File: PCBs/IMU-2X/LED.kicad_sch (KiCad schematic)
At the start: 20 parts, among them Q1 DMP2004K-7, Q2 2N7002E, Q3 2N7002E, Q4 2N7002E, Q5 2N7002E

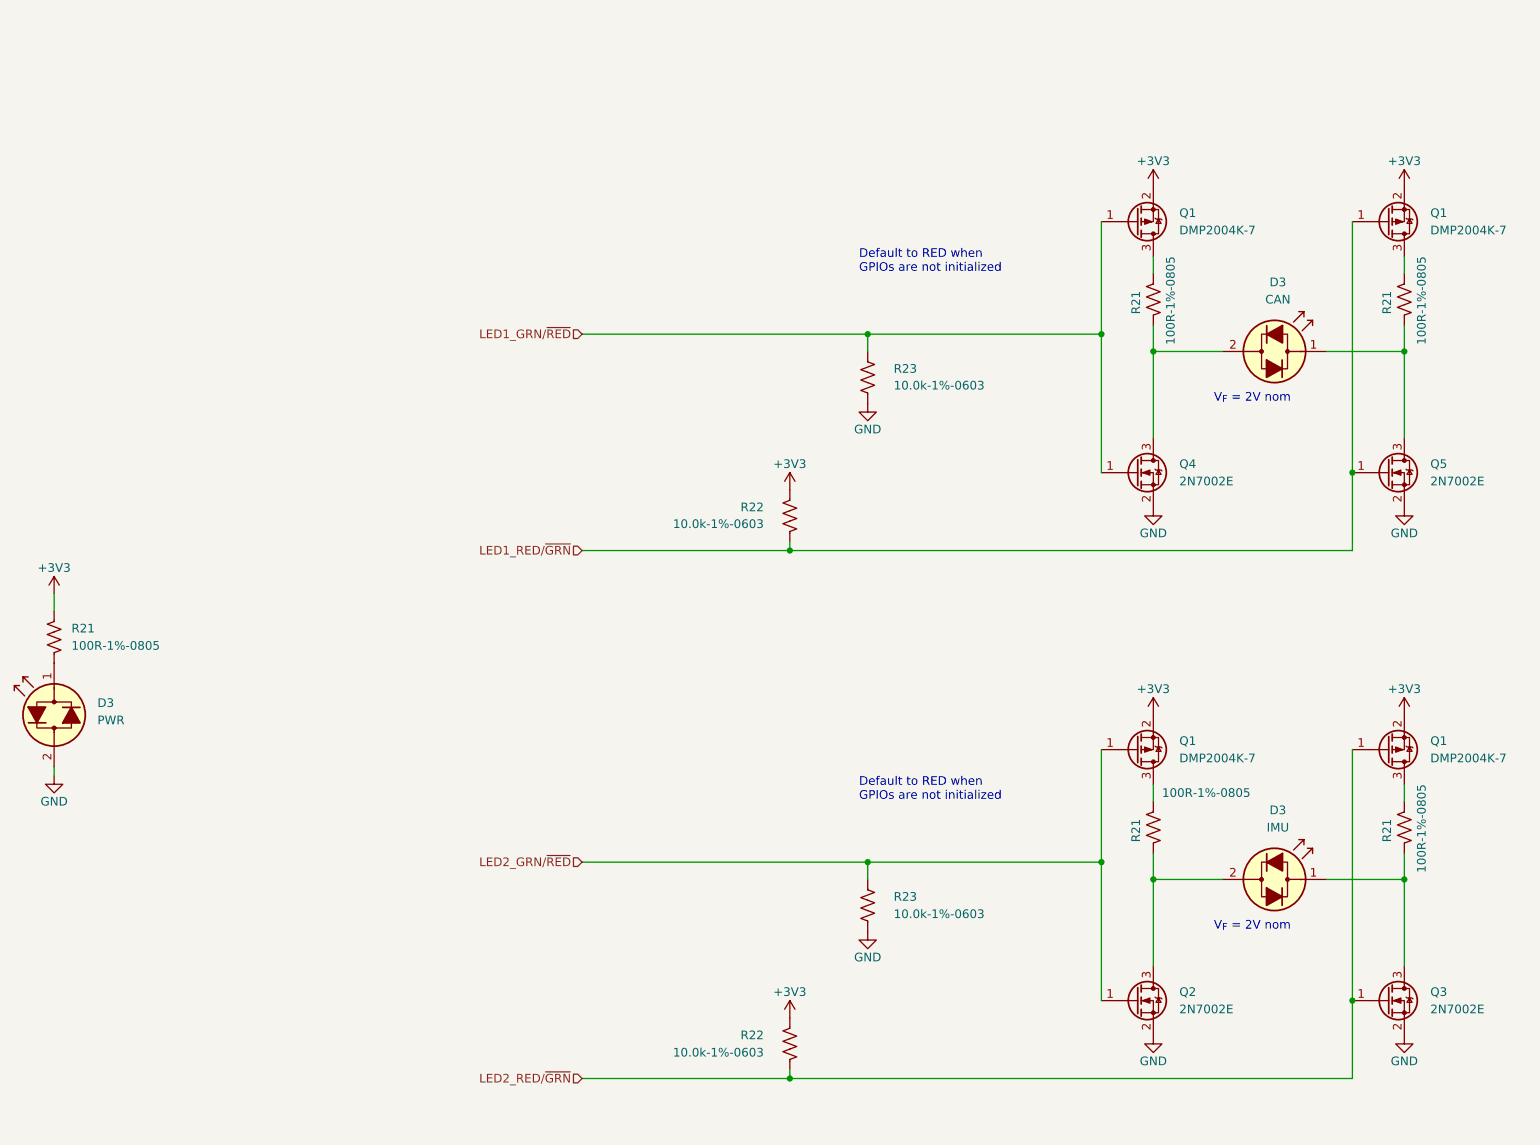
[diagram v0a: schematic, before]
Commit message: Adding IMU-2X-v2 fixes switch footprint.
Signed-off-by: Scott <sgberman1@gmail.com>
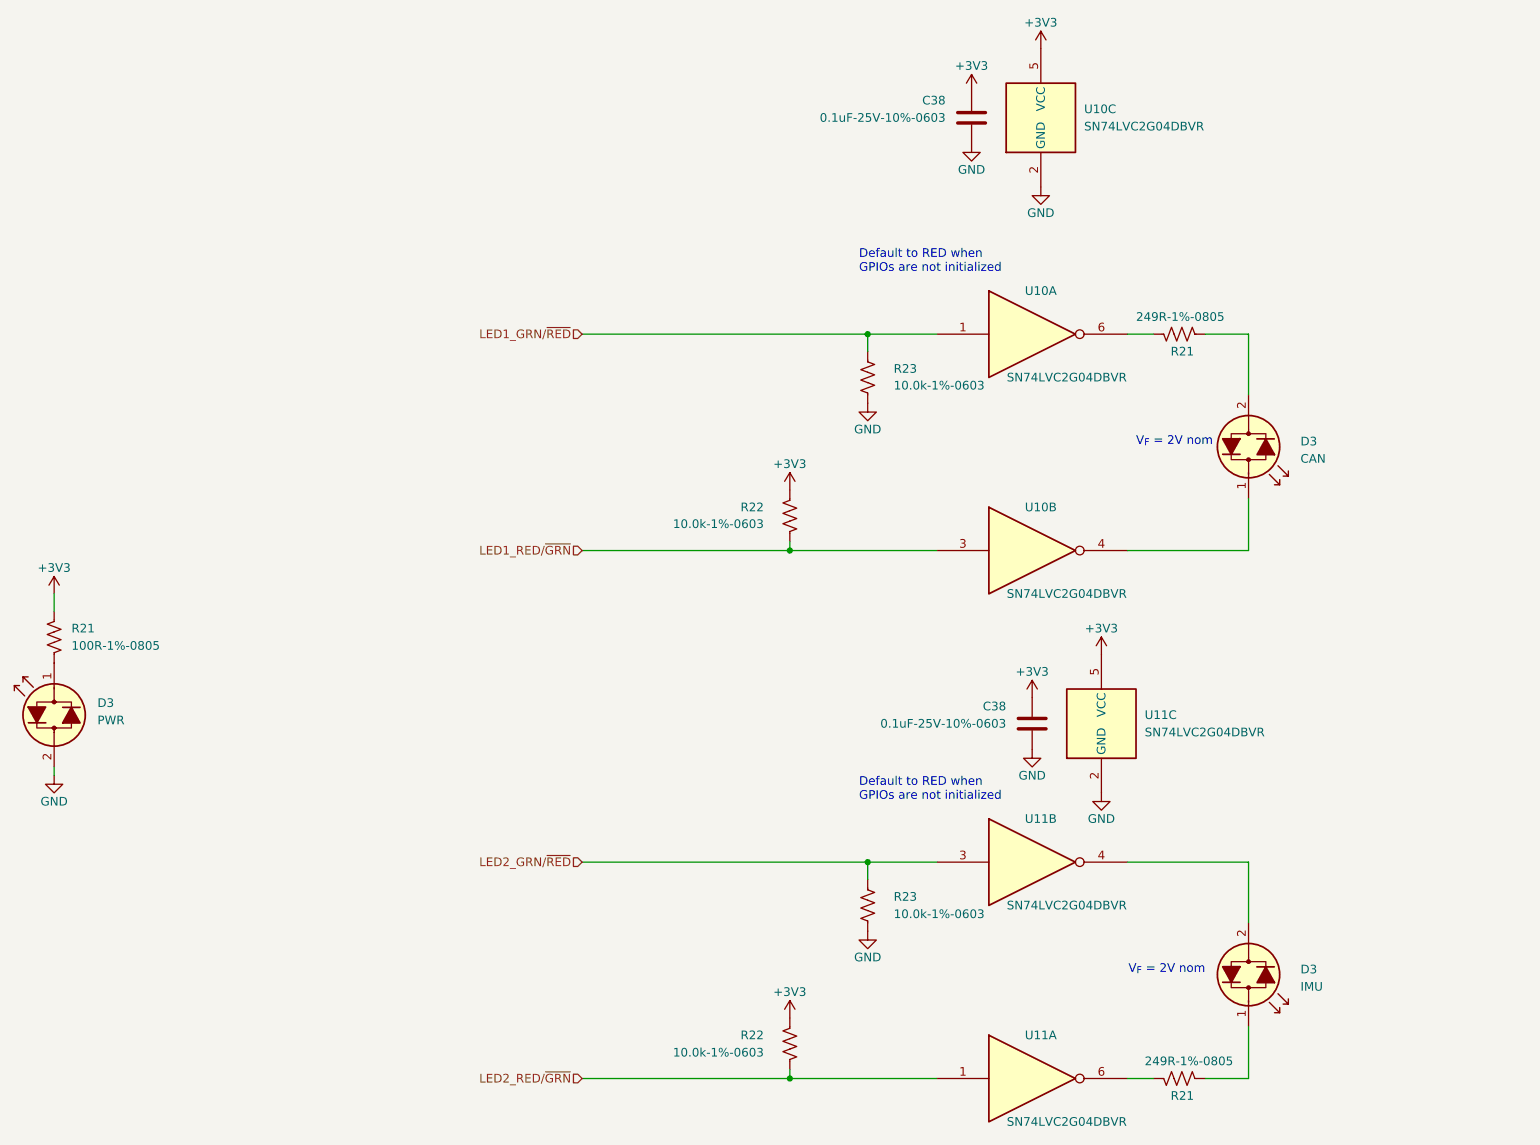
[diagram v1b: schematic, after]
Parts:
- removed Q1 (x4): DMP2004K-7, Package_TO_SOT_SMD:SOT-23, symbol Transistor_FET:BSS84
- removed Q2, Q3, Q4, Q5: 2N7002E, Package_TO_SOT_SMD:SOT-23, symbol Transistor_FET:2N7002E
- removed R21 (x2): 100R-1%-0805, Resistor_SMD:R_0805_2012Metric, symbol Device:R_US
- added C38 (x2): 0.1uF-25V-10%-0603, Capacitor_SMD:C_0603_1608Metric, symbol Device:C
- added U10, U11: SN74LVC2G04DBVR, Package_TO_SOT_SMD:SOT-23-6, symbol 74xGxx:74LVC2G04
- R21: value 100R-1%-0805 -> 249R-1%-0805; DIST P/N 311-100CRCT-ND -> 311-249CRCT-ND; MFG P/N RC0805FR-07100RL -> RC0805FR-07249RL
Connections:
- net +3V3: now also C38.1, C38.1, U10.5 (VCC), U11.5 (VCC)
- net GND: now also C38.2, C38.2, U10.2 (GND), U11.2 (GND)
- net LED1_GRN/~{RED}: now also U10.1
- net LED1_RED/~{GRN}: now also U10.3
- net LED2_GRN/~{RED}: now also U11.3
- net LED2_RED/~{GRN}: now also U11.1
- net at D3.1 (KA): now also U10.4
- net at D3.1 (KA): now also R21.1
- net at D3.2 (AK): now also U11.4; no longer R21.1
- net at R21.2: now also U11.6
- net at R21.2: now also U10.6
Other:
- moved on the sheet: D3, R21
